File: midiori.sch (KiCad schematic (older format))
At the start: 48 parts, among them J1 x68000_expansion, J2 DIN-5_180degree, J3 DIN-5_180degree, J4 DIN-5_180degree, U1 74LS245, U10 74LS393, U11 74LS74, U12 74LS30, U13 H11L1, U14 7407, U15 74LS157, U2 74LS27, U3 74LS30, U4 74LS08, U5 74LS38, U6 ym3802-x, U7 74LS32, U8 74LS04, U9 74LS10, X1 16MHz, X2 4.9152MHz

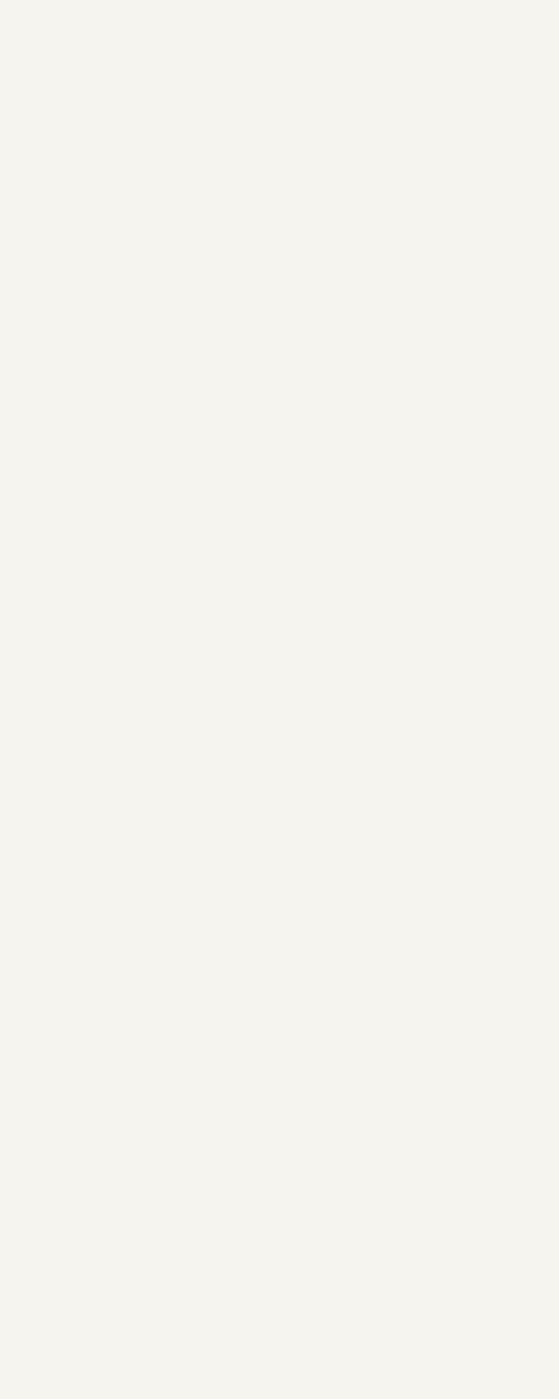
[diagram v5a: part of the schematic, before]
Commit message: ground unused inputs
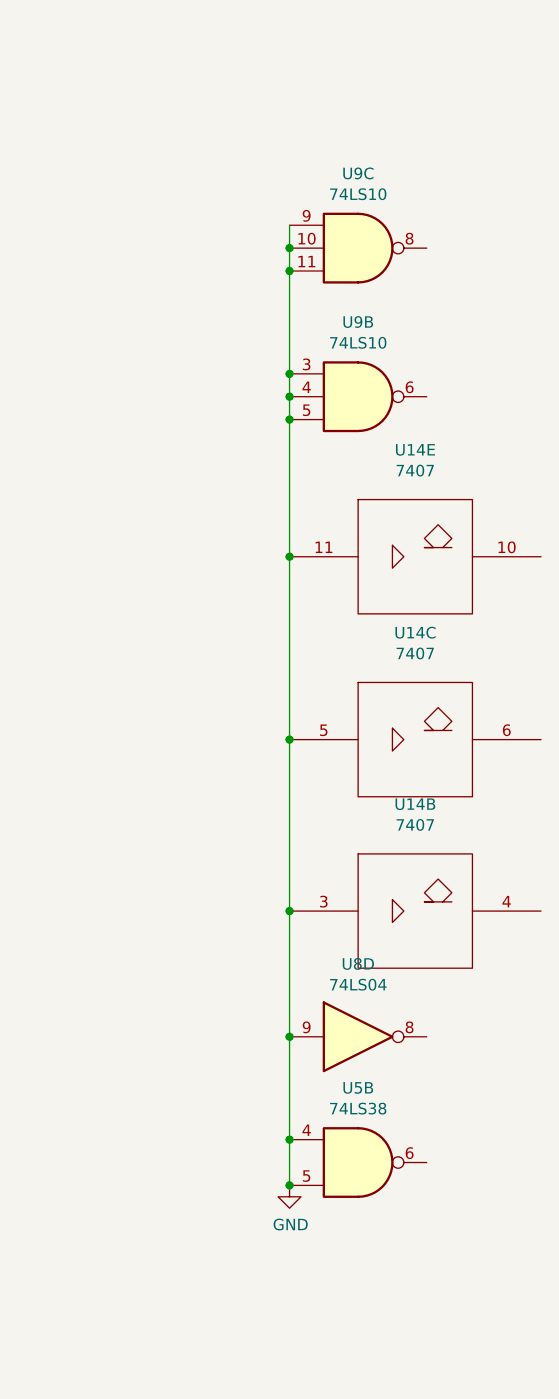
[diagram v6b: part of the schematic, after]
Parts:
- added unit 2 of U14
- added unit 3 of U14
- added unit 5 of U14
- added unit 2 of U5
- added unit 4 of U8
- added unit 2 of U9
- added unit 3 of U9
- U8: footprint Package_SO:SOIC-14_3.9x8.7mm_P1.27mm -> (none)
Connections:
- net +5V: now also U14.14 (Vcc), U14.14 (Vcc), U14.14 (Vcc)
- net GND: now also U14.11, U14.3, U14.5, U14.7 (Gnd), U14.7 (Gnd), U14.7 (Gnd), U5.4, U5.5, U8.9, U9.10, U9.11, U9.3, U9.4, U9.5, U9.9
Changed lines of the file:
@@
 F 0 "U8" H 5750 5617 50  0000 C CNN
 F 1 "74LS04" H 5750 5526 50  0000 C CNN
-F 2 "Package_SO:SOIC-14_3.9x8.7mm_P1.27mm" H 5750 5300 50  0001 C CNN
+F 2 "" H 5750 5300 50  0001 C CNN
 F 3 "http://www.ti.com/lit/gpn/sn74LS04" H 5750 5300 50  0001 C CNN
 	1    5750 5300
@@
 F 0 "U8" H 4900 7783 50  0000 C CNN
 F 1 "74LS04" H 4900 7874 50  0000 C CNN
-F 2 "Package_SO:SOIC-14_3.9x8.7mm_P1.27mm" H 4900 8100 50  0001 C CNN
+F 2 "" H 4900 8100 50  0001 C CNN
 F 3 "http://www.ti.com/lit/gpn/sn74LS04" H 4900 8100 50  0001 C CNN
 	3    4900 8100
@@
 F 0 "U8" H 6800 7683 50  0000 C CNN
 F 1 "74LS04" H 6800 7774 50  0000 C CNN
-F 2 "Package_SO:SOIC-14_3.9x8.7mm_P1.27mm" H 6800 8000 50  0001 C CNN
+F 2 "" H 6800 8000 50  0001 C CNN
 F 3 "http://www.ti.com/lit/gpn/sn74LS04" H 6800 8000 50  0001 C CNN
 	2    6800 8000
@@
 F 0 "U8" H 6800 8133 50  0000 C CNN
 F 1 "74LS04" H 6800 8224 50  0000 C CNN
-F 2 "Package_SO:SOIC-14_3.9x8.7mm_P1.27mm" H 6800 8450 50  0001 C CNN
+F 2 "" H 6800 8450 50  0001 C CNN
 F 3 "http://www.ti.com/lit/gpn/sn74LS04" H 6800 8450 50  0001 C CNN
 	6    6800 8450
@@
 F 0 "U8" H 6380 1296 50  0000 L CNN
 F 1 "74LS04" H 6380 1205 50  0000 L CNN
-F 2 "Package_SO:SOIC-14_3.9x8.7mm_P1.27mm" H 6150 1250 50  0001 C CNN
+F 2 "" H 6150 1250 50  0001 C CNN
 F 3 "http://www.ti.com/lit/gpn/sn74LS04" H 6150 1250 50  0001 C CNN
 	7    6150 1250
@@
 	1    0    0    -1
 $EndComp
+$Comp
+L 74xx:74LS38 U5
+U 2 1 5C216839
+P 15250 8200
+F 0 "U5" H 15250 8525 50  0000 C CNN
+F 1 "74LS38" H 15250 8434 50  0000 C CNN
+F 2 "" H 15250 8200 50  0001 C CNN
+F 3 "http://www.ti.com/lit/gpn/sn74LS38" H 15250 8200 50  0001 C CNN
+	2    15250 8200
+	1    0    0    -1
+$EndComp
+Wire Wire Line
+	14950 8100 14950 8300
+$Comp
+L power:GND #PWR0107
+U 1 1 5C22D82C
+P 14950 8300
+F 0 "#PWR0107" H 14950 8050 50  0001 C CNN
+F 1 "GND" H 14955 8127 50  0000 C CNN
+F 2 "" H 14950 8300 50  0001 C CNN
+F 3 "" H 14950 8300 50  0001 C CNN
+	1    14950 8300
+	1    0    0    -1
+$EndComp
+Connection ~ 14950 8300
+Connection ~ 14950 8100
+$Comp
+L 74xx:74LS04 U8
+U 4 1 5C271A56
+P 15250 7650
+F 0 "U8" H 15250 7967 50  0000 C CNN
+F 1 "74LS04" H 15250 7876 50  0000 C CNN
+F 2 "" H 15250 7650 50  0001 C CNN
+F 3 "http://www.ti.com/lit/gpn/sn74LS04" H 15250 7650 50  0001 C CNN
+	4    15250 7650
+	1    0    0    -1
+$EndComp
+Connection ~ 14950 7650
+Wire Wire Line
+	14950 7650 14950 8100
+$Comp
+L 74xx_IEEE:7407 U14
+U 2 1 5C273F31
+P 15500 7100
+F 0 "U14" H 15500 7566 50  0000 C CNN
+F 1 "7407" H 15500 7475 50  0000 C CNN
+F 2 "" H 15500 7100 50  0001 C CNN
+F 3 "" H 15500 7100 50  0001 C CNN
+	2    15500 7100
+	1    0    0    -1
+$EndComp
+Connection ~ 14950 7100
+Wire Wire Line
+	14950 7100 14950 7650
+$Comp
+L 74xx_IEEE:7407 U14
+U 3 1 5C2762D0
+P 15500 6350
+F 0 "U14" H 15500 6816 50  0000 C CNN
+F 1 "7407" H 15500 6725 50  0000 C CNN
+F 2 "" H 15500 6350 50  0001 C CNN
+F 3 "" H 15500 6350 50  0001 C CNN
+	3    15500 6350
+	1    0    0    -1
+$EndComp
+$Comp
+L 74xx_IEEE:7407 U14
+U 5 1 5C277931
+P 15500 5550
+F 0 "U14" H 15500 6016 50  0000 C CNN
+F 1 "7407" H 15500 5925 50  0000 C CNN
+F 2 "" H 15500 5550 50  0001 C CNN
+F 3 "" H 15500 5550 50  0001 C CNN
+	5    15500 5550
+	1    0    0    -1
+$EndComp
+Wire Wire Line
+	14950 6350 14950 7100
+Connection ~ 14950 6350
+Connection ~ 14950 5550
+Wire Wire Line
+	14950 5550 14950 6350
+$Comp
+L 74xx:74LS10 U9
+U 2 1 5C2CC5B7
+P 15250 4850
+F 0 "U9" H 15250 5175 50  0000 C CNN
+F 1 "74LS10" H 15250 5084 50  0000 C CNN
+F 2 "" H 15250 4850 50  0001 C CNN
+F 3 "http://www.ti.com/lit/gpn/sn74LS10" H 15250 4850 50  0001 C CNN
+	2    15250 4850
+	1    0    0    -1
+$EndComp
+Wire Wire Line
+	14950 4950 14950 5550
+$Comp
+L 74xx:74LS10 U9
+U 3 1 5C2CF2CA
+P 15250 4200
+F 0 "U9" H 15250 4525 50  0000 C CNN
+F 1 "74LS10" H 15250 4434 50  0000 C CNN
+F 2 "" H 15250 4200 50  0001 C CNN
+F 3 "http://www.ti.com/lit/gpn/sn74LS10" H 15250 4200 50  0001 C CNN
+	3    15250 4200
+	1    0    0    -1
+$EndComp
+Wire Wire Line
+	14950 4850 14950 4950
+Connection ~ 14950 4850
+Connection ~ 14950 4950
+Wire Wire Line
+	14950 4750 14950 4850
+Wire Wire Line
+	14950 4750 14950 4300
+Connection ~ 14950 4750
+Wire Wire Line
+	14950 4200 14950 4100
+Wire Wire Line
+	14950 4200 14950 4300
+Connection ~ 14950 4200
+Connection ~ 14950 4300
 $EndSCHEMATC

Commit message: rev1
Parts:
- added J5, J6, J7: AudioJack3, Connector_Audio:Jack_3.5mm_CUI_SJ1-3533NG_Horizontal, symbol Connector:AudioJack3
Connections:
- net GND: now also J5.S, J6.S, J7.S
- net at J3.4, R6.2: now also J7.R
- net at J3.5, R9.1: now also J7.T
- net at J4.4, R7.2: now also J5.R
- net at J4.5, R8.1: now also J5.T
- net at J2.4, R29.1: now also J6.R
- net at J2.5, U13.2: now also J6.T
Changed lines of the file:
@@
 	12000 4900 12000 4550
-Wire Wire Line
-	12000 4550 11800 4550
 Wire Wire Line
 	8800 4950 9600 4950
@@
 Connection ~ 14950 4200
 Connection ~ 14950 4300
+$Comp
+L Connector:AudioJack3 J7
+U 1 1 5C2C5BFE
+P 12600 4750
+F 0 "J7" H 12320 4683 50  0000 R CNN
+F 1 "AudioJack3" H 12320 4774 50  0000 R CNN
+F 2 "Connector_Audio:Jack_3.5mm_CUI_SJ1-3533NG_Horizontal" H 12600 4750 50  0001 C CNN
+F 3 "~" H 12600 4750 50  0001 C CNN
+	1    12600 4750
+	-1   0    0    1
+$EndComp
+$Comp
+L Connector:AudioJack3 J5
+U 1 1 5C2C7414
+P 12550 5750
+F 0 "J5" H 12270 5683 50  0000 R CNN
+F 1 "AudioJack3" H 12270 5774 50  0000 R CNN
+F 2 "Connector_Audio:Jack_3.5mm_CUI_SJ1-3533NG_Horizontal" H 12550 5750 50  0001 C CNN
+F 3 "~" H 12550 5750 50  0001 C CNN
+	1    12550 5750
+	-1   0    0    1
+$EndComp
+$Comp
+L Connector:AudioJack3 J6
+U 1 1 5C2C7C33
+P 12550 6750
+F 0 "J6" H 12270 6683 50  0000 R CNN
+F 1 "AudioJack3" H 12270 6774 50  0000 R CNN
+F 2 "Connector_Audio:Jack_3.5mm_CUI_SJ1-3533NG_Horizontal" H 12550 6750 50  0001 C CNN
+F 3 "~" H 12550 6750 50  0001 C CNN
+	1    12550 6750
+	-1   0    0    1
+$EndComp
+Wire Wire Line
+	11200 6400 11200 6350
+Connection ~ 11200 6350
+Wire Wire Line
+	12350 6850 11850 6850
+Wire Wire Line
+	11850 6850 11850 6350
+Wire Wire Line
+	11850 6350 11200 6350
+Wire Wire Line
+	12350 5850 12050 5850
+Wire Wire Line
+	12050 5850 12050 5350
+Wire Wire Line
+	12050 5350 11500 5350
+Wire Wire Line
+	11500 5350 11500 5300
+Connection ~ 11500 5300
+Wire Wire Line
+	11500 4350 12100 4350
+Wire Wire Line
+	12100 4350 12100 4850
+Wire Wire Line
+	12100 4850 12400 4850
+Connection ~ 11500 4350
+Wire Wire Line
+	11200 4550 11200 4100
+Wire Wire Line
+	11200 4100 12200 4100
+Wire Wire Line
+	12200 4100 12200 4750
+Wire Wire Line
+	12200 4750 12400 4750
+Connection ~ 11200 4550
+Wire Wire Line
+	11200 5500 11200 5150
+Wire Wire Line
+	11200 5150 12150 5150
+Wire Wire Line
+	12150 5150 12150 5750
+Wire Wire Line
+	12150 5750 12350 5750
+Connection ~ 11200 5500
+Wire Wire Line
+	10900 6550 10900 6100
+Wire Wire Line
+	10900 6100 11950 6100
+Wire Wire Line
+	11950 6100 11950 6750
+Wire Wire Line
+	11950 6750 12350 6750
+Connection ~ 10900 6550
+Wire Wire Line
+	11750 6550 12350 6550
+Wire Wire Line
+	12350 6550 12350 6650
+Connection ~ 11750 6550
+Wire Wire Line
+	11950 5500 12350 5500
+Wire Wire Line
+	12350 5500 12350 5650
+Connection ~ 11950 5500
+Wire Wire Line
+	12400 4550 12400 4650
+Wire Wire Line
+	11800 4550 12000 4550
+Connection ~ 12000 4550
+Wire Wire Line
+	12000 4550 12400 4550
 $EndSCHEMATC

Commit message: bugfixes
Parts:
- added unit 2 of U3
- U3, U4: footprint Package_SO:SOIC-14_3.9x8.7mm_P1.27mm -> (none)
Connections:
- net A16 is gone; now on net AB16: J1.B22 (AB16)
- net A17 is gone; now on net AB17: J1.B23 (AB17)
- net A18 is gone; now on net AB18: J1.B24 (AB18)
- net A19 is gone; now on net AB19: J1.B25 (AB19)
- net A20 is gone; now on net AB20: J1.B26 (AB20)
- net A21 is gone; now on net AB21: J1.B27 (AB21)
- net A22 is gone; now on net AB22: J1.B28 (AB22)
- net A23 is gone; now on net AB23: J1.B29 (AB23)
- net +5V: now also U3.14 (VCC)
- net GND: now also U4.10, U3.7 (GND); no longer U14.11, U14.3, U14.5, U8.9, U9.10, U9.11, U9.3, U9.4, U9.5, U9.9
- net at U3.8: now also U8.9; no longer U4.10
- net at U7.13: now also U4.11; no longer U4.8
- net at U4.9: now also U14.11, U14.3, U14.5, U9.10, U9.11, U9.3, U9.4, U9.5, U9.9; no longer U4.11
- net at U12.11, U12.12: now also U8.8
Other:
- moved on the sheet: U8D
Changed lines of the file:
@@
 AB15
 Text Label 2300 5450 0    50   ~ 0
-A16
+AB16
 Text Label 2300 5550 0    50   ~ 0
-A17
+AB17
 Text Label 2300 5650 0    50   ~ 0
-A18
+AB18
 Text Label 2300 5750 0    50   ~ 0
-A19
+AB19
 Text Label 2300 5850 0    50   ~ 0
-A20
+AB20
 Text Label 2300 5950 0    50   ~ 0
-A21
+AB21
 Text Label 2300 6050 0    50   ~ 0
-A22
+AB22
 Text Label 2300 6150 0    50   ~ 0
-A23
+AB23
 Wire Wire Line
 	2300 8150 2450 8150
@@
 F 0 "U4" H 3600 4975 50  0000 C CNN
 F 1 "74LS08" H 3600 4884 50  0000 C CNN
-F 2 "Package_SO:SOIC-14_3.9x8.7mm_P1.27mm" H 3600 4650 50  0001 C CNN
+F 2 "" H 3600 4650 50  0001 C CNN
 F 3 "http://www.ti.com/lit/gpn/sn74LS08" H 3600 4650 50  0001 C CNN
 	1    3600 4650
@@
 F 0 "U4" H 3600 5475 50  0000 C CNN
 F 1 "74LS08" H 3600 5384 50  0000 C CNN
-F 2 "Package_SO:SOIC-14_3.9x8.7mm_P1.27mm" H 3600 5150 50  0001 C CNN
+F 2 "" H 3600 5150 50  0001 C CNN
 F 3 "http://www.ti.com/lit/gpn/sn74LS08" H 3600 5150 50  0001 C CNN
 	2    3600 5150
@@
 Text Label 3300 5250 2    50   ~ 0
 IACK2
-$Comp
-L 74xx:74LS08 U4
-U 3 1 5BFE9128
-P 5700 4700
-F 0 "U4" H 5700 5025 50  0000 C CNN
-F 1 "74LS08" H 5700 4934 50  0000 C CNN
-F 2 "Package_SO:SOIC-14_3.9x8.7mm_P1.27mm" H 5700 4700 50  0001 C CNN
-F 3 "http://www.ti.com/lit/gpn/sn74LS08" H 5700 4700 50  0001 C CNN
-	3    5700 4700
-	1    0    0    -1
-$EndComp
-Wire Wire Line
-	5300 5150 5300 4600
-Wire Wire Line
-	5300 4600 5400 4600
 $Comp
 L 74xx:74LS157 U15
@@
 	1    0    0    -1
 $EndComp
-Wire Wire Line
-	6150 4950 6000 4950
-Wire Wire Line
-	6000 4950 6000 4700
 Text Label 6150 4750 2    50   ~ 0
 AS
@@
 F 0 "U4" H 4480 1296 50  0000 L CNN
 F 1 "74LS08" H 4480 1205 50  0000 L CNN
-F 2 "Package_SO:SOIC-14_3.9x8.7mm_P1.27mm" H 4250 1250 50  0001 C CNN
+F 2 "" H 4250 1250 50  0001 C CNN
 F 3 "http://www.ti.com/lit/gpn/sn74LS08" H 4250 1250 50  0001 C CNN
 	5    4250 1250
@@
 F 0 "U3" H 4650 4275 50  0000 C CNN
 F 1 "74LS30" H 4650 4184 50  0000 C CNN
-F 2 "Package_SO:SOIC-14_3.9x8.7mm_P1.27mm" H 4650 3750 50  0001 C CNN
+F 2 "" H 4650 3750 50  0001 C CNN
 F 3 "http://www.ti.com/lit/gpn/sn74LS30" H 4650 3750 50  0001 C CNN
 	1    4650 3750
@@
 	4700 5150 4700 5250
 Wire Wire Line
-	5400 4800 5050 4800
-Wire Wire Line
-	5050 4800 5050 3750
-Wire Wire Line
 	5050 3750 4950 3750
 Wire Wire Line
@@
 	9700 750  10000 750
 Wire Wire Line
-	1450 750  3000 750
-Wire Wire Line
-	1450 1750 3000 1750
+	1450 750  2300 750
+Wire Wire Line
+	1450 1750 2300 1750
 Connection ~ 6550 9150
 Connection ~ 6550 9750
@@
 L 74xx:74LS04 U8
 U 4 1 5C271A56
-P 15250 7650
-F 0 "U8" H 15250 7967 50  0000 C CNN
-F 1 "74LS04" H 15250 7876 50  0000 C CNN
-F 2 "" H 15250 7650 50  0001 C CNN
-F 3 "http://www.ti.com/lit/gpn/sn74LS04" H 15250 7650 50  0001 C CNN
-	4    15250 7650
-	1    0    0    -1
-$EndComp
-Connection ~ 14950 7650
-Wire Wire Line
-	14950 7650 14950 8100
+P 5350 4200
+F 0 "U8" H 5350 4517 50  0000 C CNN
+F 1 "74LS04" H 5350 4426 50  0000 C CNN
+F 2 "" H 5350 4200 50  0001 C CNN
+F 3 "http://www.ti.com/lit/gpn/sn74LS04" H 5350 4200 50  0001 C CNN
+	4    5350 4200
+	1    0    0    -1
+$EndComp
 $Comp
 L 74xx_IEEE:7407 U14
@@
 $EndComp
 Connection ~ 14950 7100
-Wire Wire Line
-	14950 7100 14950 7650
 $Comp
 L 74xx_IEEE:7407 U14
@@
 Wire Wire Line
 	12000 4550 12400 4550
+Wire Wire Line
+	5050 4200 5050 3750
+Wire Wire Line
+	5300 5150 5300 4950
+Wire Wire Line
+	5300 4950 6150 4950
+Wire Wire Line
+	14950 7100 14950 7550
+Wire Wire Line
+	4350 4950 4350 5050
+Wire Wire Line
+	4350 5050 4600 5050
+Wire Wire Line
+	4600 5050 4600 4800
+Wire Wire Line
+	4600 4800 5650 4800
+Wire Wire Line
+	5650 4800 5650 4200
+Connection ~ 4350 4950
+$Comp
+L 74xx:74LS30 U3
+U 2 1 5C5A84CB
+P 2300 1250
+F 0 "U3" H 2530 1296 50  0000 L CNN
+F 1 "74LS30" H 2530 1205 50  0000 L CNN
+F 2 "" H 2300 1250 50  0001 C CNN
+F 3 "http://www.ti.com/lit/gpn/sn74LS30" H 2300 1250 50  0001 C CNN
+	2    2300 1250
+	1    0    0    -1
+$EndComp
+Connection ~ 2300 750
+Wire Wire Line
+	2300 750  3000 750
+Connection ~ 2300 1750
+Wire Wire Line
+	2300 1750 3000 1750
+$Comp
+L 74xx:74LS08 U4
+U 3 1 5C5B9871
+P 15250 7650
+F 0 "U4" H 15250 7975 50  0000 C CNN
+F 1 "74LS08" H 15250 7884 50  0000 C CNN
+F 2 "" H 15250 7650 50  0001 C CNN
+F 3 "http://www.ti.com/lit/gpn/sn74LS08" H 15250 7650 50  0001 C CNN
+	3    15250 7650
+	1    0    0    -1
+$EndComp
+Wire Wire Line
+	14950 7750 14950 8100
 $EndSCHEMATC
